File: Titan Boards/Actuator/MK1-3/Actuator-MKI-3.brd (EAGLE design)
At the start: 101.6 x 50.8 mm, 57 parts, among them U1 DRV8816PWPR, U2 MBRB2060CTT4G, U3 MBRB2060CTT4G, U4 MBRB2060CTT4G, U5 MBRB2060CTT4G, U6 MBRB2060CTT4G, U7 MBRB2060CTT4G

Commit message: Actuator MK1-3 updates
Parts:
- R10: value 1K -> 10K
- R11: value 150 -> 1.5K
- moved R7 155.6 mm to (34.7, 53.1), flipped to the bottom, turned to 90 degrees
- moved R6 146.7 mm to (29.3, 53.1), flipped to the bottom, turned to 90 degrees
- moved R8 139.4 mm to (10.2, 53.1), flipped to the bottom, turned to 90 degrees
- moved R14 134.9 mm to (60.1, 54.0), turned to 180 degrees
- moved CHARGING 133.8 mm to (54.2, 54.0), turned to 270 degrees
- moved R17 126.3 mm to (60.1, 50.8), turned to 180 degrees
- moved R3 125.3 mm to (7.49, 53.1), flipped to the bottom, turned to 90 degrees
- moved R22 120.8 mm to (32.0, 53.1), flipped to the bottom, turned to 90 degrees
- moved R24 120.6 mm to (26.6, 53.1), flipped to the bottom, turned to 90 degrees
- moved R44 120.5 mm to (-1.91, 45.0), flipped to the bottom, turned to 270 degrees
- moved R25 120.3 mm to (21.1, 53.1), flipped to the bottom, turned to 90 degrees
- moved R27 118.0 mm to (12.9, 53.1), flipped to the bottom, turned to 90 degrees
- moved R19 117.4 mm to (37.5, 53.1), flipped to the bottom, turned to 90 degrees
- moved R43 115.6 mm to (-4.32, 45.0), flipped to the bottom, turned to 90 degrees
- moved DISCHARGING 112.2 mm to (54.2, 50.8), turned to 270 degrees
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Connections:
- new net VPROPI: U$9.P$6, U1.15
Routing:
- net AGND: track 16.9 -> 64.0 mm, vias 7 -> 8
- net TORPEDO2_GATE: track 0.00 -> 15.4 mm, vias 0 -> 1
- net DROPPER2_GATE: track 0.00 -> 12.0 mm, vias 0 -> 1
- net MOTOR_EN: track 0.00 -> 12.0 mm, vias 0 -> 1
- net PWM_DRIVER2: track 0.00 -> 11.3 mm, vias 0 -> 1
- net COIL_4_GATE: track 0.00 -> 10.6 mm, vias 0 -> 1
- net COIL_2_GATE: track 0.00 -> 10.2 mm, vias 0 -> 1
- net ARM_TORPEDO: track 0.00 -> 9.78 mm, vias 0 -> 1
- net COIL_3_GATE: track 0.00 -> 7.59 mm, vias 0 -> 1
- net PWM_DRIVER1: track 0.00 -> 7.35 mm, vias 0 -> 1
- net TORPEDO1_GATE: track 0.00 -> 6.60 mm, vias 0 -> 1
- net COIL_1_GATE: track 0.00 -> 5.47 mm, vias 0 -> 1
- net DROPPER1_GATE: track 0.00 -> 4.91 mm, vias 0 -> 1
- net N$10: track 5.40 -> 2.61 mm, vias 1 -> 0
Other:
- board size 101.6 x 50.8 mm -> 101.6 x 55.9 mm

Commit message: Actuator MKIII updates'
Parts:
- removed C20, C4: UVK1E223MRD, UVK1E223MRD:CAP_UFW_25X50_NCH
- added U$1: 31059104, 31059104:31059104
- moved R10 100.1 mm to (45.7, 50.9), turned to 180 degrees
- moved R11 94.8 mm to (41.9, 50.9), turned to 180 degrees
- moved R9 19.1 mm to (7.37, 41.8)
- moved R12 14.7 mm to (5.33, 41.8)
- moved R43 11.8 mm to (7.24, 47.2)
- moved R44 7.43 mm to (5.21, 47.2)
- moved Q2 4.77 mm to (2.67, 47.2)
- moved Q3 1.57 mm to (2.79, 41.8)
- moved CHARGING 1.02 mm to (54.1, 53.0)
- moved R14 1.02 mm to (59.9, 53.0)
- moved Q18 0.28 mm to (4.95, 30.5)
- moved Q6 0.13 mm to (13.0, 30.4)
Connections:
- net +24V: now also U$1.P$1, U$1.P$2; no longer C20.1, C4.1
- net AGND: now also U$1.P$3, U$1.P$4; no longer C20.2, C4.2
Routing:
- net +3V3: track 0.00 -> 84.5 mm, vias 0 -> 2
- net MOTOR_EN: track 12.0 -> 87.3 mm, vias 1 -> 4
- net DROPPER1_GATE: track 4.91 -> 77.9 mm, vias 1 -> 2
- net VPROPI: track 0.00 -> 71.7 mm, vias 0 -> 2
- net PWM_DRIVER1: track 7.35 -> 77.8 mm, vias 1 -> 2
- net ARM_TORPEDO: track 9.78 -> 78.3 mm, vias 1 -> 4
- net DROPPER2_GATE: track 12.0 -> 80.4 mm, vias 1 -> 2
- net PWM_DRIVER2: track 11.3 -> 75.2 mm, vias 1 -> 2
- net AGND: track 64.0 -> 7.54 mm, vias 8 -> 127
- net TORPEDO2_GATE: track 15.4 -> 61.4 mm, vias 1 -> 2
- net SDA: track 0.00 -> 44.4 mm, vias 0 -> 1
- net V_DIV: track 0.00 -> 35.1 mm, vias 0 -> 2
- net SCL: track 0.00 -> 32.5 mm, vias 0 -> 1
- net COIL_4_GATE: track 10.6 -> 38.3 mm, vias 1 -> 2
- net COIL_2_GATE: track 10.2 -> 34.6 mm, vias 1 -> 2
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- added copper zone on layer 2, net +12V
- added copper zone on layer 2, net +24V
- added copper zone on layer 15, net AGND
- added copper zone on layer 2, net AGND

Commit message: Actuator MK3 for Review
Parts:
- removed U$9: JTAG-SMD, JTAG-SMD:JTAG-SMD
- added U$2: JTAG-SMD, JTAG-SMD:JTAG-SMD
- moved R18 18.9 mm to (37.3, 53.1)
- moved R7 16.4 mm to (18.3, 53.1)
- moved R21 8.05 mm to (31.9, 53.1)
- moved R6 5.53 mm to (23.8, 53.1)
- moved R19 2.86 mm to (34.6, 53.1)
- moved R22 2.83 mm to (29.2, 53.1)
- moved C5 2.80 mm to (95.1, 30.2)
- moved 120 2.03 mm to (95.2, 39.9)
- moved CHARGING 0.13 mm to (54.2, 53.0)
- moved Q18 0.13 mm to (4.95, 30.4)
- moved R17 0.13 mm to (59.9, 50.8)
- moved R24 0.10 mm to (26.5, 53.1)
- moved R25 0.07 mm to (21.0, 53.1)
- flipped BACKPLANE_CONN to the top
- flipped CLAW_CONN to the top
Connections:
- net +3V3: now also U$2.P$1, U$2.P$11; no longer U$9.P$1, U$9.P$11
- net AGND: now also U$2.P$10, U$2.P$20; no longer U$9.P$10, U$9.P$20
- net ARM_TORPEDO: now also U$2.P$6; no longer U$9.P$18
- net COIL_1_GATE: now also R24.1, U$2.P$14; no longer R6.1, U$9.P$4
- net COIL_2_GATE: now also R6.1, U$2.P$4; no longer R24.1, U$9.P$14
- net COIL_3_GATE: now also R25.1, U$2.P$15; no longer R7.1, U$9.P$5
- net COIL_4_GATE: now also R7.1, U$2.P$5; no longer R25.1, U$9.P$15
- net DROPPER1_GATE: now also U$2.P$3; no longer U$9.P$3
- net DROPPER2_GATE: now also U$2.P$13; no longer U$9.P$13
- net MOTOR_EN: now also U$2.P$16; no longer U$9.P$16
- net PWM_DRIVER1: now also U$2.P$9; no longer U$9.P$9
- net PWM_DRIVER2: now also U$2.P$19; no longer U$9.P$19
- net SCL: now also U$2.P$7; no longer U$9.P$17
- net SDA: now also U$2.P$17; no longer U$9.P$7
- net TORPEDO1_GATE: now also U$2.P$2; no longer U$9.P$2
- net TORPEDO2_GATE: now also U$2.P$12; no longer U$9.P$12
- net VPROPI: now also U$2.P$18; no longer U$9.P$6
- net V_DIV: now also U$2.P$8; no longer U$9.P$8
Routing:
- net TORPEDO1_GATE: track 28.4 -> 54.8 mm
- net MOTOR_EN: track 87.3 -> 71.1 mm
- net TORPEDO2_GATE: track 61.4 -> 46.6 mm
- net VPROPI: track 71.7 -> 59.1 mm
- net PWM_DRIVER2: track 75.2 -> 63.8 mm
- net SCL: track 32.5 -> 42.8 mm
- net COIL_3_GATE: track 30.9 -> 40.4 mm
- net V_DIV: track 35.1 -> 40.9 mm
- net AGND: track 7.54 -> 1.82 mm, vias 127 -> 124
- net DROPPER2_GATE: track 80.4 -> 76.5 mm
- net COIL_4_GATE: track 38.3 -> 34.8 mm
- net +3V3: track 84.5 -> 81.1 mm
- net ARM_TORPEDO: track 78.3 -> 81.5 mm
- net SDA: track 44.4 -> 41.7 mm
- net DROPPER1_GATE: track 77.9 -> 80.3 mm
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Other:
- board text added: "+12V"
- board text added: "+24V"
- board text added: "+3V3"
- board text added: "+5V"
- board text added: "+V"
- board text added: "1"
- board text added: "2"
- board text added: "3"
- board text added: "4"
- board text added: "ACTUATOR BOARD"
- board text added: "AGND"
- board text added: "ARM TORP"
- board text added: "All 10K"
- board text added: "COIL2 GATE"
- board text added: "COIL4 GATE"
- board text added: "COIL_1"
- board text added: "COIL_2"
- board text added: "COIL_3"
- board text added: "COIL_4"
- board text added: "Claw"
- board text added: "DROP1 GATE"
- board text added: "DROP_1"
- board text added: "DROP_2"
- board text added: "EXTRA5"
- board text added: "EXTRA6"
- board text added: "MOTOR EN"
- board text added: "PWM DRV1"
- board text added: "PWM DRV2"
- board text added: "PWM_OUT1"
- board text added: "PWM_OUT2"
- board text added: "SCL"
- board text added: "SDA"
- board text added: "TORP1 GATE"
- board text added: "TORP_1"
- board text added: "TORP_2"
- board text added: "Torpedo Coils"
- board text added: "VDIV"
- board text added: "VPROPI"

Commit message: Tempest Actuator Updates
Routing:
- net PWM_DRIVER1: track 77.5 -> 80.4 mm
- net VPROPI: track 59.1 -> 59.8 mm

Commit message: Tempest Actuator Board Review Revisions
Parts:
- removed U6, U7: MBRB2060CTT4G, DPAK2:D2PAK3-4_9P65X10P29_ONS
- added Q1, Q4: (no value), SparkFun-DiscreteSemi:SOT23-3
- moved Q18 8.00 mm to (13.0, 30.5)
- moved Q6 8.00 mm to (4.95, 30.5)
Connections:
- removed net EXTRA5: BACKPLANE_CONN.3
- removed net EXTRA6: BACKPLANE_CONN.1
- net +3V3: now also BACKPLANE_CONN.1; no longer BACKPLANE_CONN.2
- net AGND: now also Q1.3; no longer U7.4
- net N$5: now also Q1.1; no longer U7.3
- net N$6: now also Q1.2, Q4.1; no longer U6.3, U7.1
- net N$7: now also Q4.3; no longer U6.4
- net PWM_OUT2: now also CLAW_CONN.2; no longer CLAW_CONN.3
- net TORPEDO2: now also TORPEDO_CONN.4; no longer TORPEDO_CONN.2
- net V+: now also Q4.2; no longer U6.1
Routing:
- net AGND: track 1.82 -> 53.1 mm, vias 124 -> 139
- net N$7: track 0.00 -> 13.8 mm
- net DROPPER2_GATE: track 76.5 -> 66.4 mm
- net DROPPER1_GATE: track 80.3 -> 70.3 mm
- net +3V3: track 81.1 -> 77.1 mm
- net V_DIV: track 40.9 -> 38.4 mm
- net N$35: track 11.3 -> 9.23 mm, vias 2 -> 0
- net +24V: track 16.6 -> 15.1 mm
- net N$33: track 15.2 -> 16.5 mm
- net N$6: track 10.7 -> 9.49 mm
- net N$5: track 2.94 -> 2.30 mm
- removed copper zone on layer 1, net N$7
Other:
- board text added: "COIL1 GATE"
- board text added: "COIL3 GATE"
- board text added: "DROP2 GATE"
- board text added: "TORP2 GATE"

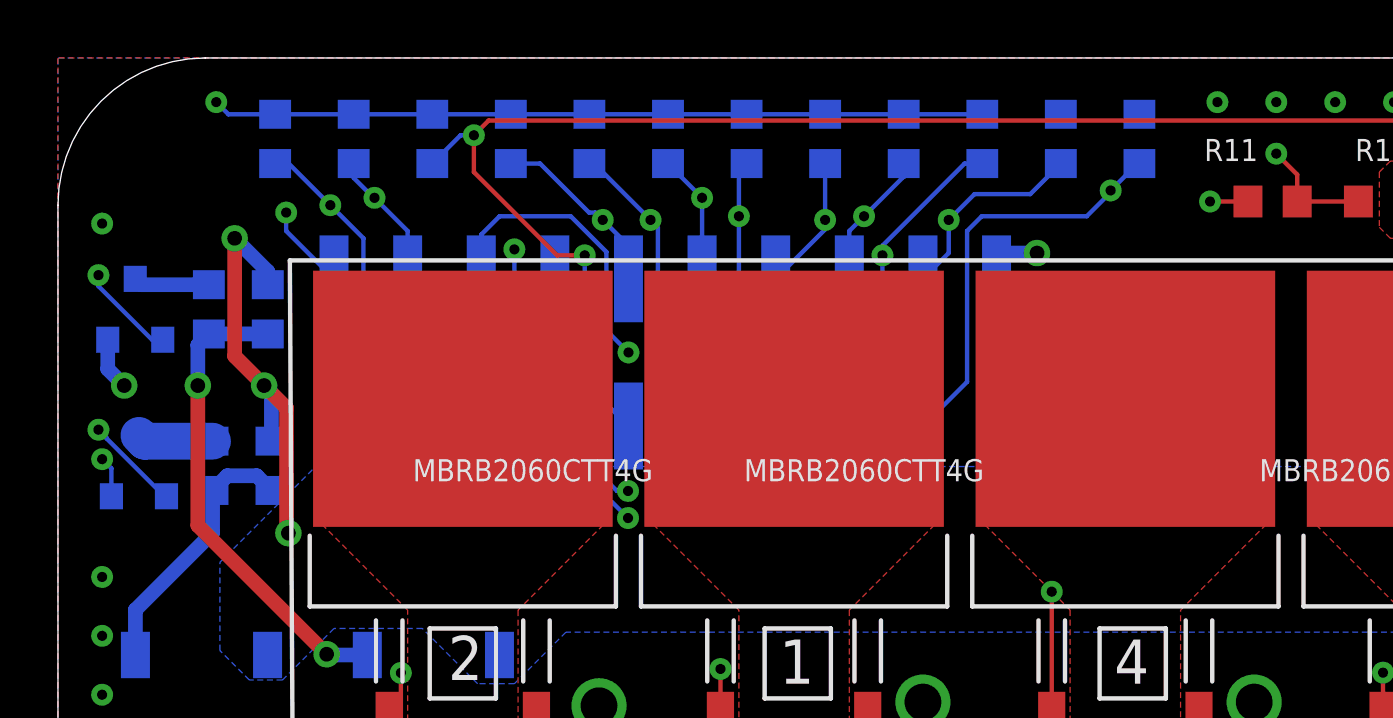
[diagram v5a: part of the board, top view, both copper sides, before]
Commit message: Minor changes to actuator board
Changed some minor things on actuator board. Ready to order -PB
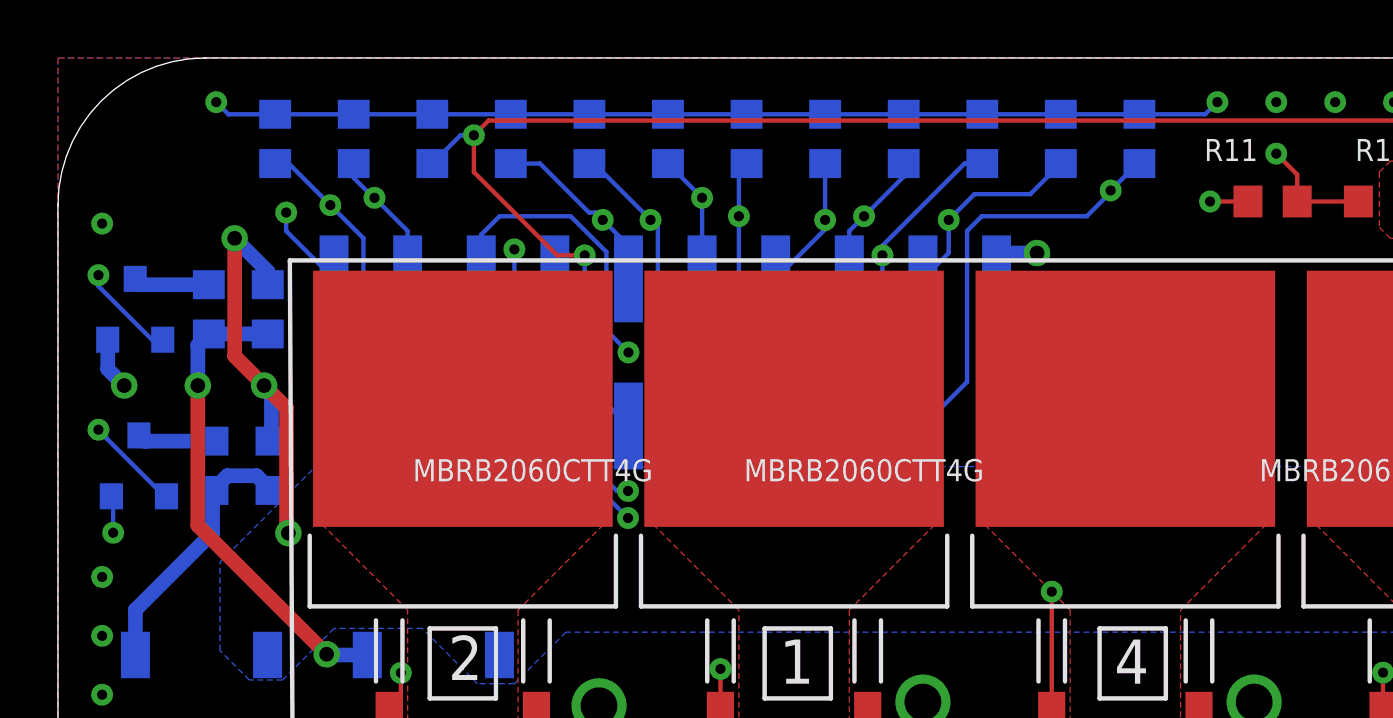
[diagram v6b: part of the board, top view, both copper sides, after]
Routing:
- net AGND: track 53.1 -> 61.3 mm
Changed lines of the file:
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@@
 <via x="1.524" y="35.941" extent="1-16" drill="0.35"/>
 <via x="1.524" y="37.973" extent="1-16" drill="0.35"/>
-<via x="1.524" y="42.037" extent="1-16" drill="0.35"/>
+<via x="1.905" y="39.497" extent="1-16" drill="0.35"/>
 <via x="1.524" y="50.165" extent="1-16" drill="0.35"/>
 <contactref element="U$2" pad="P$10"/>
@@
 <wire x1="9.525" y1="48.26" x2="7.874" y2="49.911" width="0.1524" layer="16"/>
 <wire x1="7.874" y1="49.911" x2="7.874" y2="50.546" width="0.1524" layer="16"/>
-<wire x1="1.844" y1="40.7572" x2="1.844" y2="41.717" width="0.1524" layer="16"/>
-<wire x1="1.844" y1="41.717" x2="1.524" y2="42.037" width="0.1524" layer="16"/>
+<wire x1="1.844" y1="40.7572" x2="1.905" y2="40.6962" width="0.1524" layer="16"/>
+<wire x1="1.905" y1="40.6962" x2="1.905" y2="39.497" width="0.1524" layer="16"/>
 <via x="58.928" y="23.876" extent="1-16" drill="0.508" diameter="0.508"/>
 <via x="60.325" y="23.876" extent="1-16" drill="0.508" diameter="0.508"/>
@@
 <via x="92.964" y="54.356" extent="1-16" drill="0.35"/>
 <via x="94.869" y="54.356" extent="1-16" drill="0.35"/>
+<wire x1="31.89273125" y1="53.936" x2="34.6038125" y2="53.936" width="0.1524" layer="16"/>
+<wire x1="34.6038125" y1="53.936" x2="37.31489375" y2="53.936" width="0.1524" layer="16"/>
+<wire x1="37.31489375" y1="53.936" x2="39.585" y2="53.936" width="0.1524" layer="16"/>
+<wire x1="39.585" y1="53.936" x2="40.005" y2="54.356" width="0.1524" layer="16"/>
 </signal>
 <signal name="SDA">
@@
 <contactref element="R12" pad="1"/>
 <contactref element="Q3" pad="3"/>
-<wire x1="5.334" y1="42.6572" x2="2.994" y2="42.6572" width="1.27" layer="16"/>
-<wire x1="2.994" y1="42.6572" x2="2.794" y2="42.8572" width="1.27" layer="16"/>
+<wire x1="5.334" y1="42.6572" x2="2.994" y2="42.6572" width="0.508" layer="16"/>
+<wire x1="2.994" y1="42.6572" x2="2.794" y2="42.8572" width="0.508" layer="16"/>
 </signal>
 <signal name="TORPEDO2">
